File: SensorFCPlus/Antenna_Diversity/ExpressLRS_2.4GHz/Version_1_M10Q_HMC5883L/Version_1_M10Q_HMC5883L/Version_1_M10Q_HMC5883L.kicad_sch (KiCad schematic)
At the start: 7 parts, among them U1 HMC5883L

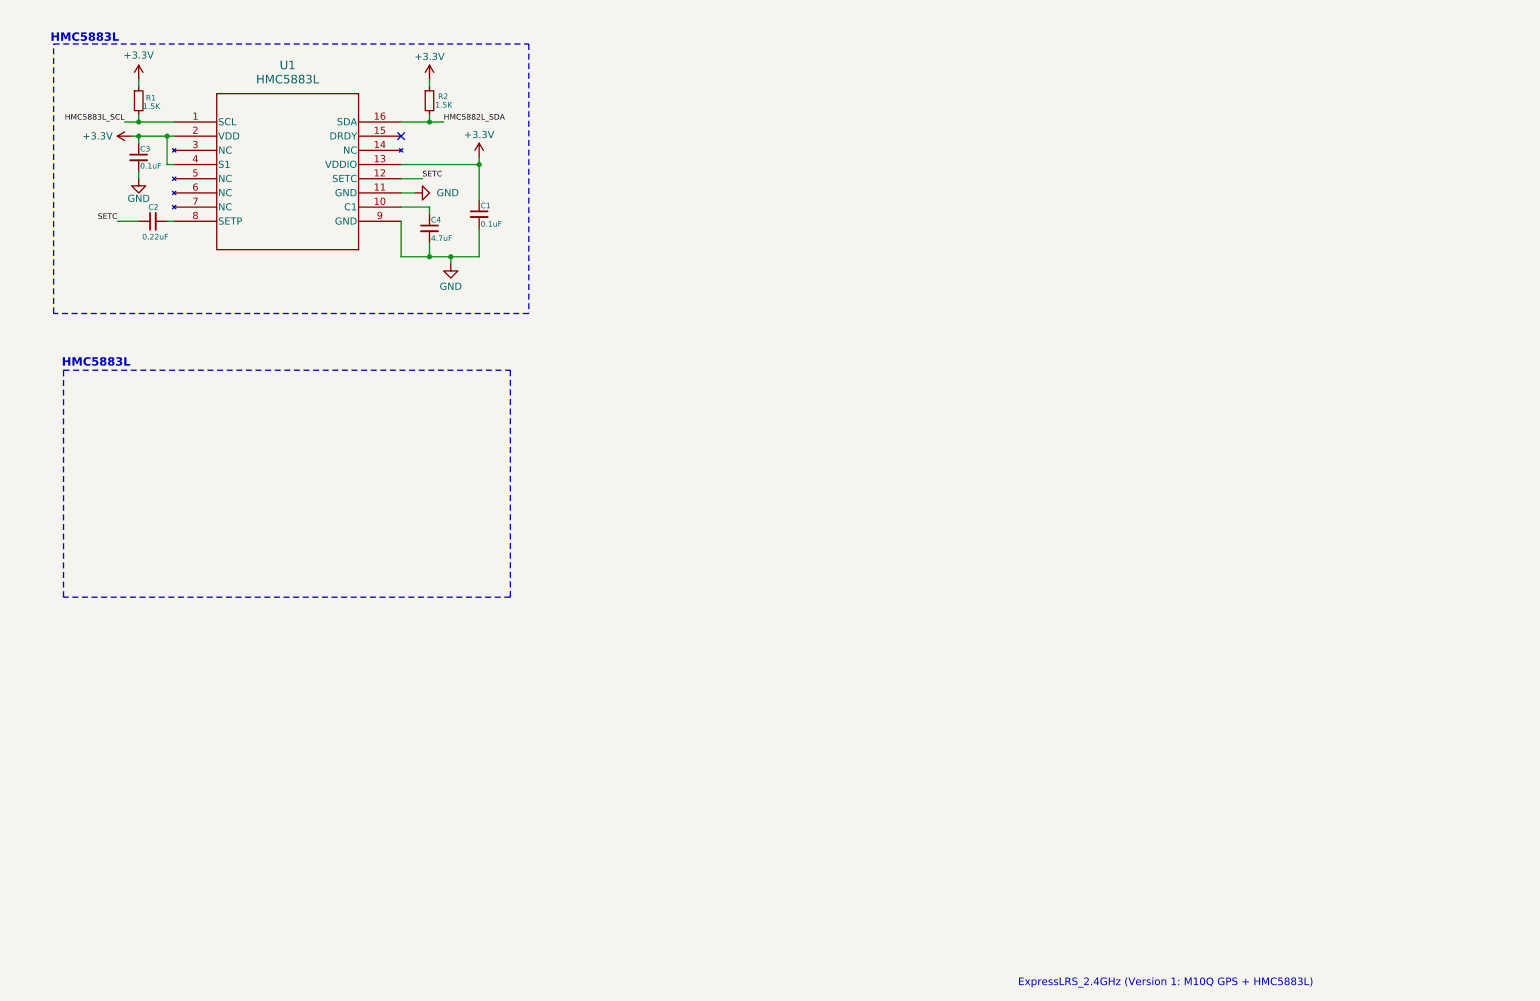
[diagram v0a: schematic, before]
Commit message: Update KiCad schematic and project files for ExpressLRS 2.4GHz modules (Version 1 and 2) and add new components (ESP8285, SE2431L, SX1280)
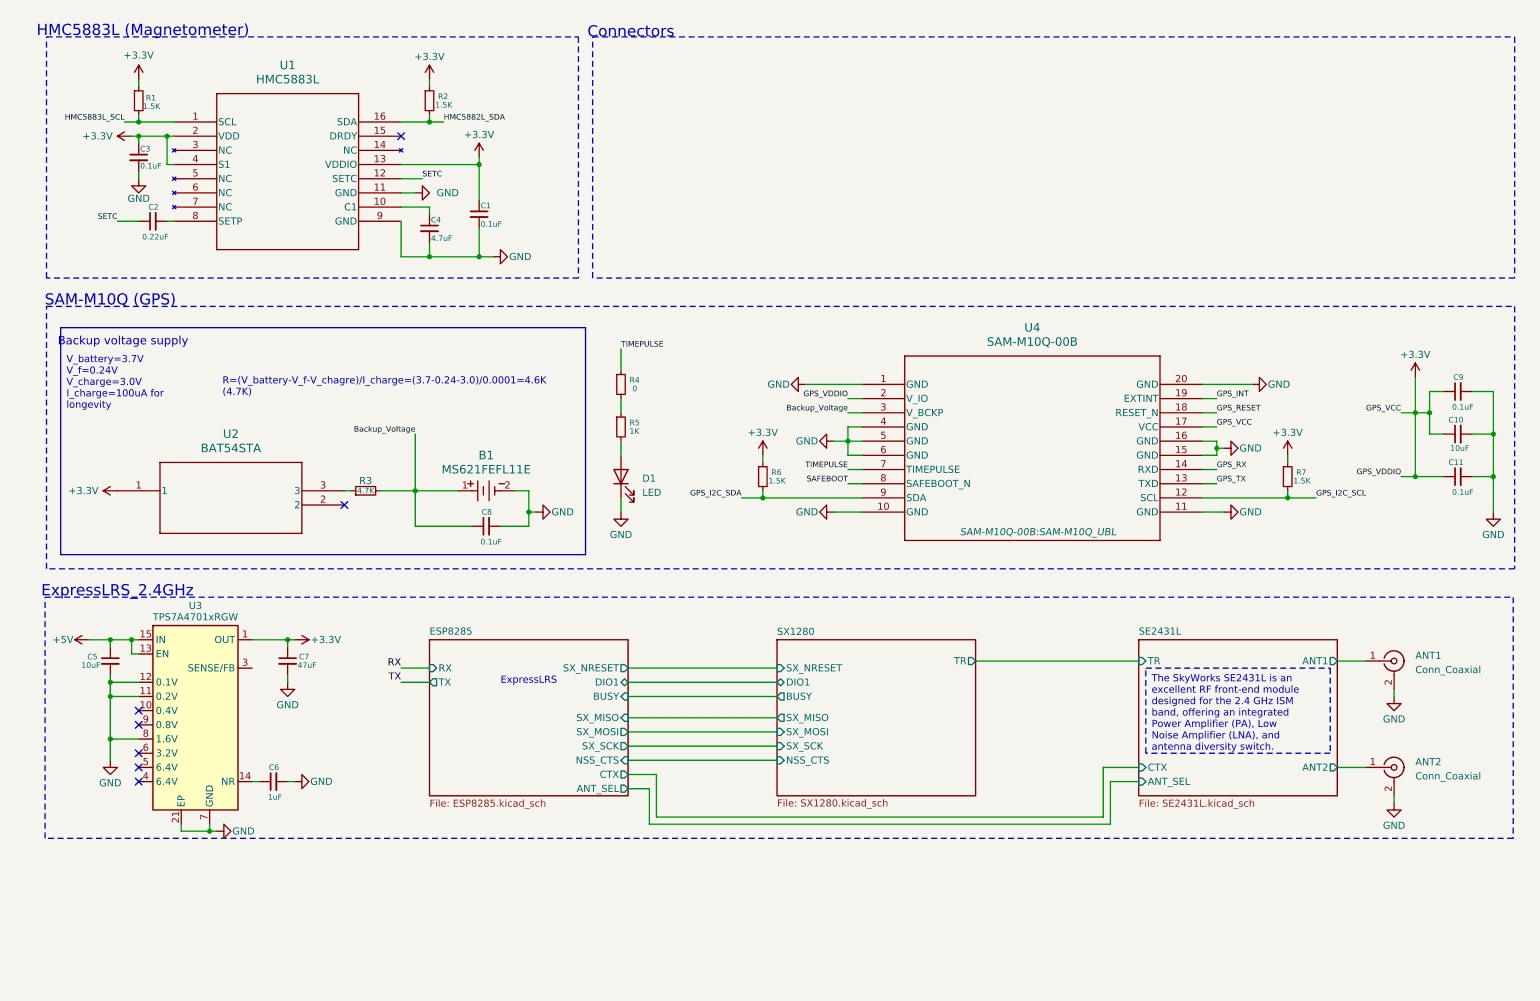
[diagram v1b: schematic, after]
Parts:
- added ANT1, ANT2: Conn_Coaxial, Connector_Coaxial:U.FL_Hirose_U.FL-R-SMT-1_Vertical, symbol Connector:Conn_Coaxial
- added B1: MS621FEFL11E, MS621FE-FL11E:MS621FE-FL11E, symbol MS621FE-FL11E:MS621FEFL11E
- added C10: 10uF, ECASD40J106M055K00:ECASD40J106M055K00, symbol Device:C_Small
- added C11, C8, C9: 0.1uF, Capacitor_SMD:C_0805_2012Metric_Pad1.18x1.45mm_HandSolder, symbol Device:C_Small
- added C5: 10uF, Capacitor_SMD:C_0805_2012Metric_Pad1.18x1.45mm_HandSolder, symbol Device:C_Small
- added C6: 1uF, Capacitor_SMD:C_0805_2012Metric_Pad1.18x1.45mm_HandSolder, symbol Device:C_Small
- added C7: 47uF, Capacitor_SMD:C_0805_2012Metric_Pad1.18x1.45mm_HandSolder, symbol Device:C_Small
- added D1: LED, LED_SMD:LED_0805_2012Metric_Pad1.15x1.40mm_HandSolder, symbol Device:LED
- added R3: 4.7K, Resistor_SMD:R_0805_2012Metric_Pad1.20x1.40mm_HandSolder, symbol Device:R_Small
- added R4: 0, Resistor_SMD:R_0805_2012Metric_Pad1.20x1.40mm_HandSolder, symbol Device:R_Small
- added R5: 1K, Resistor_SMD:R_0805_2012Metric_Pad1.20x1.40mm_HandSolder, symbol Device:R_Small
- added R6, R7: 1.5K, Resistor_SMD:R_0805_2012Metric_Pad1.20x1.40mm_HandSolder, symbol Device:R_Small
- added U2: BAT54STA, SOT23_BAT54STA_1P7XP85_DIO, symbol BAT54STA:BAT54STA
- added U3: TPS7A4701xRGW, Package_DFN_QFN:Texas_RGW0020A_VQFN-20-1EP_5x5mm_P0.65mm_EP3.15x3.15mm_ThermalVias, symbol Regulator_Linear:TPS7A4701xRGW
- added U4: SAM-M10Q-00B, SAM-M10Q-00B:SAM-M10Q_UBL, symbol SAM-M10Q-00B:SAM-M10Q-00B
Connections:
- net +3.3V: now also C10.1, C11.1, C7.1, C9.1, R6.1, R7.1, U2.1, U3.1 (OUT), U3.20 (OUT), U4.17 (VCC), U4.2 (V_IO)
- net GND: now also ANT1.2 (Ext), ANT2.2 (Ext), B1.2, C10.2, C11.2, C5.2, C6.2, C7.2, C8.2, C9.2, D1.1 (K), U3.11 (0.2V), U3.12 (0.1V), U3.21 (EP), U3.7 (GND), U3.8 (1.6V), U4.1 (GND), U4.10 (GND), U4.11 (GND), U4.15 (GND), U4.16 (GND), U4.20 (GND), U4.4 (GND), U4.5 (GND), U4.6 (GND)
- new net: D1.2 (A), R5.2
- new net: R4.2, R5.1
- new net: C6.1, U3.14 (NR)
- new net: R3.1, U2.3
- new net +5V: C5.1, U3.13 (EN), U3.15 (IN), U3.16 (IN)
- new net Backup_Voltage: B1.1, C8.1, R3.2, U4.3 (V_BCKP)
- new net GPS_I2C_SCL: R7.2, U4.12 (SCL)
- new net GPS_I2C_SDA: R6.2, U4.9 (SDA)
- new net GPS_INT: U4.19 (EXTINT)
- new net GPS_RESET: U4.18 (RESET_N)
- new net GPS_RX: U4.14 (RXD)
- new net GPS_TX: U4.13 (TXD)
- new net SAFEBOOT: U4.8 (SAFEBOOT_N)
- new net SE2431L/ANT1: ANT1.1 (In)
- new net SE2431L/ANT2: ANT2.1 (In)
- new net TIMEPULSE: R4.1, U4.7 (TIMEPULSE)
- no-connect marks 1 -> 7
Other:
- added sheet ESP8285 (ESP8285.kicad_sch)
- added sheet SE2431L (SE2431L.kicad_sch)
- added sheet SX1280 (SX1280.kicad_sch)
- note added: "Backup voltage supply"
- note added: "Connectors"
- note added: "ExpressLRS"
- note added: "ExpressLRS_2.4GHz"
- note added: "HMC5883L (Magnetometer)"
- note added: "SAM-M10Q (GPS)"
- note removed: "ExpressLRS_2.4GHz (Version 1: M10Q GPS + HMC5883L)"
- note removed: "HMC5883L"
- company: (none) -> https://github.com/Paschalis
- title: (none) -> Version 1 (GPS:M10Q, MAG:HMC5883L, ELRS:2.4GHz_RX)

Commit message: Updated README and V1 M10Q HMC5883L KiCad files, added documentation and media
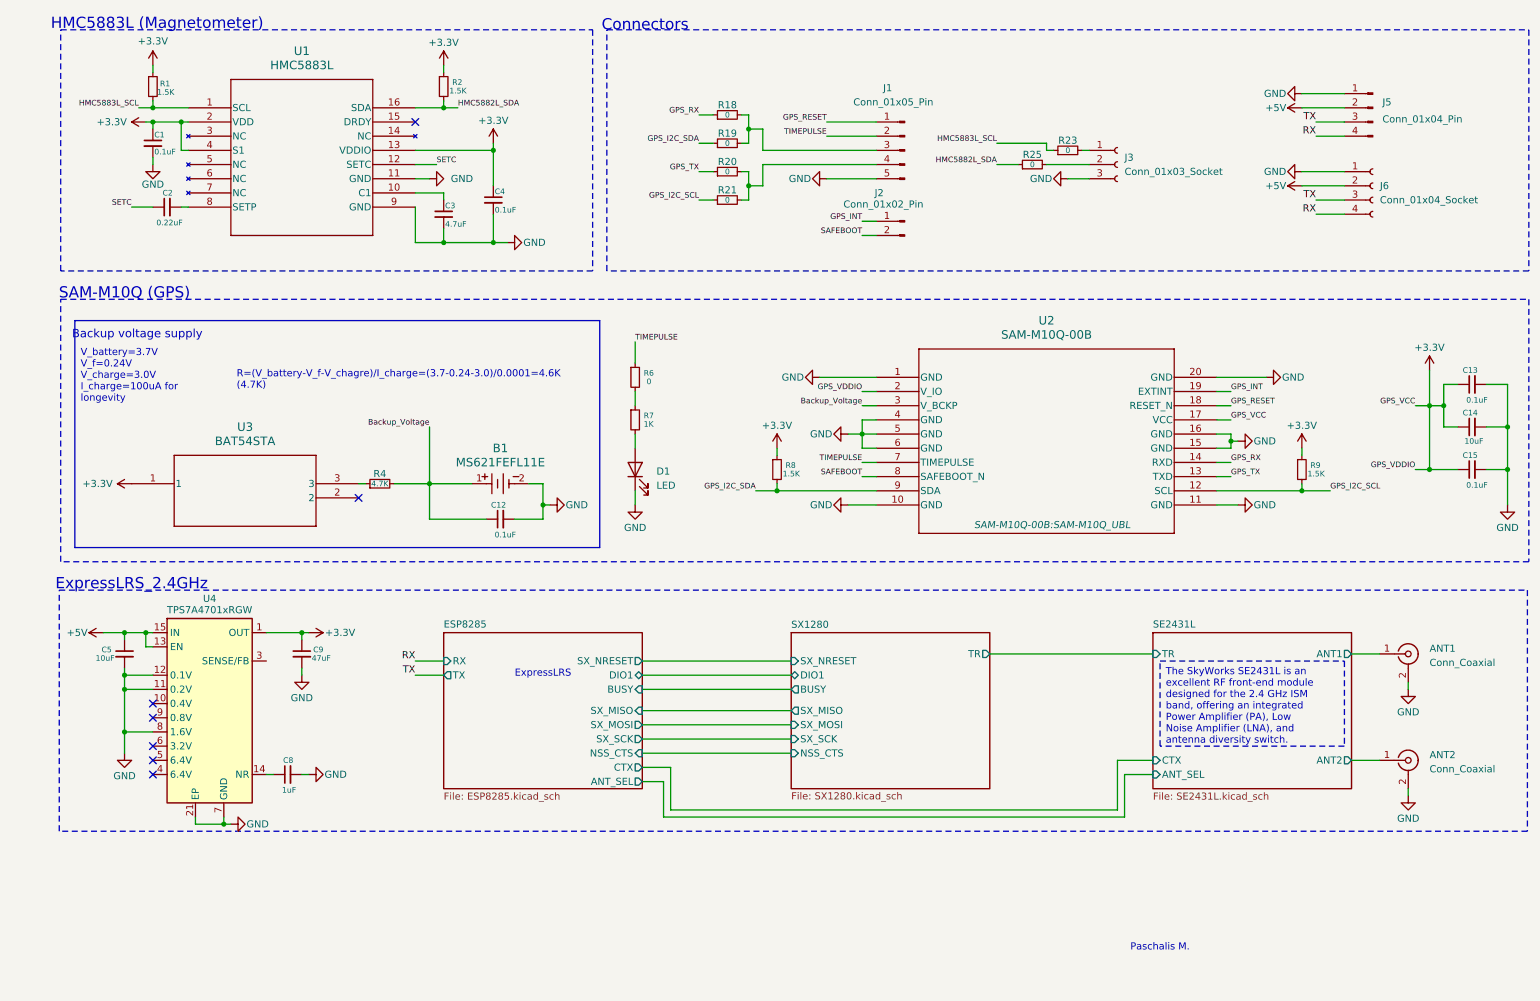
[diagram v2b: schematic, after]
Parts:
- removed C10: 10uF, ECASD40J106M055K00:ECASD40J106M055K00, symbol Device:C_Small
- removed C11: 0.1uF, Capacitor_SMD:C_0805_2012Metric_Pad1.18x1.45mm_HandSolder, symbol Device:C_Small
- removed C6: 1uF, Capacitor_SMD:C_0805_2012Metric_Pad1.18x1.45mm_HandSolder, symbol Device:C_Small
- removed C7: 47uF, Capacitor_SMD:C_0805_2012Metric_Pad1.18x1.45mm_HandSolder, symbol Device:C_Small
- removed R3: 4.7K, Resistor_SMD:R_0805_2012Metric_Pad1.20x1.40mm_HandSolder, symbol Device:R_Small
- removed R5: 1K, Resistor_SMD:R_0805_2012Metric_Pad1.20x1.40mm_HandSolder, symbol Device:R_Small
- removed U2: BAT54STA, SOT23_BAT54STA_1P7XP85_DIO, symbol BAT54STA:BAT54STA
- removed U3: TPS7A4701xRGW, Package_DFN_QFN:Texas_RGW0020A_VQFN-20-1EP_5x5mm_P0.65mm_EP3.15x3.15mm_ThermalVias, symbol Regulator_Linear:TPS7A4701xRGW
- removed U4: SAM-M10Q-00B, SAM-M10Q-00B:SAM-M10Q_UBL, symbol SAM-M10Q-00B:SAM-M10Q-00B
- added C12, C13, C15: 0.1uF, Capacitor_SMD:C_0805_2012Metric_Pad1.18x1.45mm_HandSolder, symbol Device:C_Small
- added C14: 10uF, ECASD40J106M055K00:ECASD40J106M055K00, symbol Device:C_Small
- added J1: Conn_01x05_Pin, Connector_PinHeader_2.00mm:PinHeader_1x05_P2.00mm_Vertical, symbol Connector:Conn_01x05_Pin
- added J2: Conn_01x02_Pin, Connector_PinHeader_2.00mm:PinHeader_1x02_P2.00mm_Vertical, symbol Connector:Conn_01x02_Pin
- added J3: Conn_01x03_Socket, Connector_JST:JST_GH_SM03B-GHS-TB_1x03-1MP_P1.25mm_Horizontal, symbol Connector:Conn_01x03_Socket
- added J5: Conn_01x04_Pin, Connector_JST:JST_GH_SM04B-GHS-TB_1x04-1MP_P1.25mm_Horizontal, symbol Connector:Conn_01x04_Pin
- added J6: Conn_01x04_Socket, Connector_Harwin:Harwin_M20-89004xx_1x04_P2.54mm_Horizontal, symbol Connector:Conn_01x04_Socket
- added R18, R19, R20, R21, R23, R25: 0, Resistor_SMD:R_0603_1608Metric_Pad0.98x0.95mm_HandSolder, symbol Device:R_Small
- added R8, R9: 1.5K, Resistor_SMD:R_0805_2012Metric_Pad1.20x1.40mm_HandSolder, symbol Device:R_Small
- added U2: SAM-M10Q-00B, SAM-M10Q-00B:SAM-M10Q_UBL, symbol SAM-M10Q-00B:SAM-M10Q-00B
- added U3: BAT54STA, BAT54STA:BAT54STA, symbol BAT54STA:BAT54STA
- added U4: TPS7A4701xRGW, Package_DFN_QFN:Texas_RGW0020A_VQFN-20-1EP_5x5mm_P0.65mm_EP3.15x3.15mm_ThermalVias, symbol Regulator_Linear:TPS7A4701xRGW
- C3: value 0.1uF -> 4.7uF
- C4: value 4.7uF -> 0.1uF
- C8: value 0.1uF -> 1uF
- C9: value 0.1uF -> 47uF
- R4: value 0 -> 4.7K
- R6: value 1.5K -> 0
- R7: value 1.5K -> 1K
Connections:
- net +3.3V: now also C4.1, C13.1, C14.1, C15.1, R8.1, R9.1, U2.17 (VCC), U2.2 (V_IO), U3.1, U4.1 (OUT), U4.20 (OUT); no longer C3.1, R6.1, R7.1
- net +5V: now also J5.2 (Pin_2), J6.2 (Pin_2), U4.13 (EN), U4.15 (IN), U4.16 (IN)
- net Backup_Voltage: now also R4.2, C12.1, U2.3 (V_BCKP); no longer C8.1
- net GND: now also C12.2, C13.2, C14.2, C15.2, J1.5 (Pin_5), J3.3 (Pin_3), J5.1 (Pin_1), J6.1 (Pin_1), U2.1 (GND), U2.10 (GND), U2.11 (GND), U2.15 (GND), U2.16 (GND), U2.20 (GND), U2.4 (GND), U2.5 (GND), U2.6 (GND), U4.11 (0.2V), U4.12 (0.1V), U4.21 (EP), U4.7 (GND), U4.8 (1.6V)
- net GPS_I2C_SCL: now also R21.1, R9.2, U2.12 (SCL); no longer R7.2
- net GPS_I2C_SDA: now also R19.1, R8.2, U2.9 (SDA); no longer R6.2
- net GPS_INT: now also J2.1 (Pin_1), U2.19 (EXTINT)
- net GPS_RESET: now also J1.1 (Pin_1), U2.18 (RESET_N)
- net GPS_RX: now also R18.1, U2.14 (RXD)
- net GPS_TX: now also R20.1, U2.13 (TXD)
- net HMC5882L_SDA: now also R25.1
- net HMC5883L_SCL: now also R23.1
- net RX: now also J5.4 (Pin_4), J6.4 (Pin_4)
- net SAFEBOOT: now also J2.2 (Pin_2), U2.8 (SAFEBOOT_N)
- net TIMEPULSE: now also R6.1, J1.2 (Pin_2), U2.7 (TIMEPULSE); no longer R4.1
- net TX: now also J5.3 (Pin_3), J6.3 (Pin_3)
- net at U1.10 (C1): now also C3.1; no longer C4.1
- net at D1.2 (A): now also R7.2
- new net: J1.3 (Pin_3), R18.2, R19.2
- new net: R4.1, U3.3
- new net: R6.2, R7.1
- new net: J1.4 (Pin_4), R20.2, R21.2
- new net: C8.1, U4.14 (NR)
- new net: J3.2 (Pin_2), R25.2
- new net: J3.1 (Pin_1), R23.2
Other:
- note added: "Paschalis M."
- title: Version 1 (GPS:M10Q, MAG:HMC5883L, ELRS:2.4GHz_RX) -> Version 2 (GPS:M10Q, MAG:HMC5883L, ELRS:2.4GHz_RX)
